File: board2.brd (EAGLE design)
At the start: 100 x 80 mm, 77 parts, among them Q1 7.68MHz, Q2 16MHz

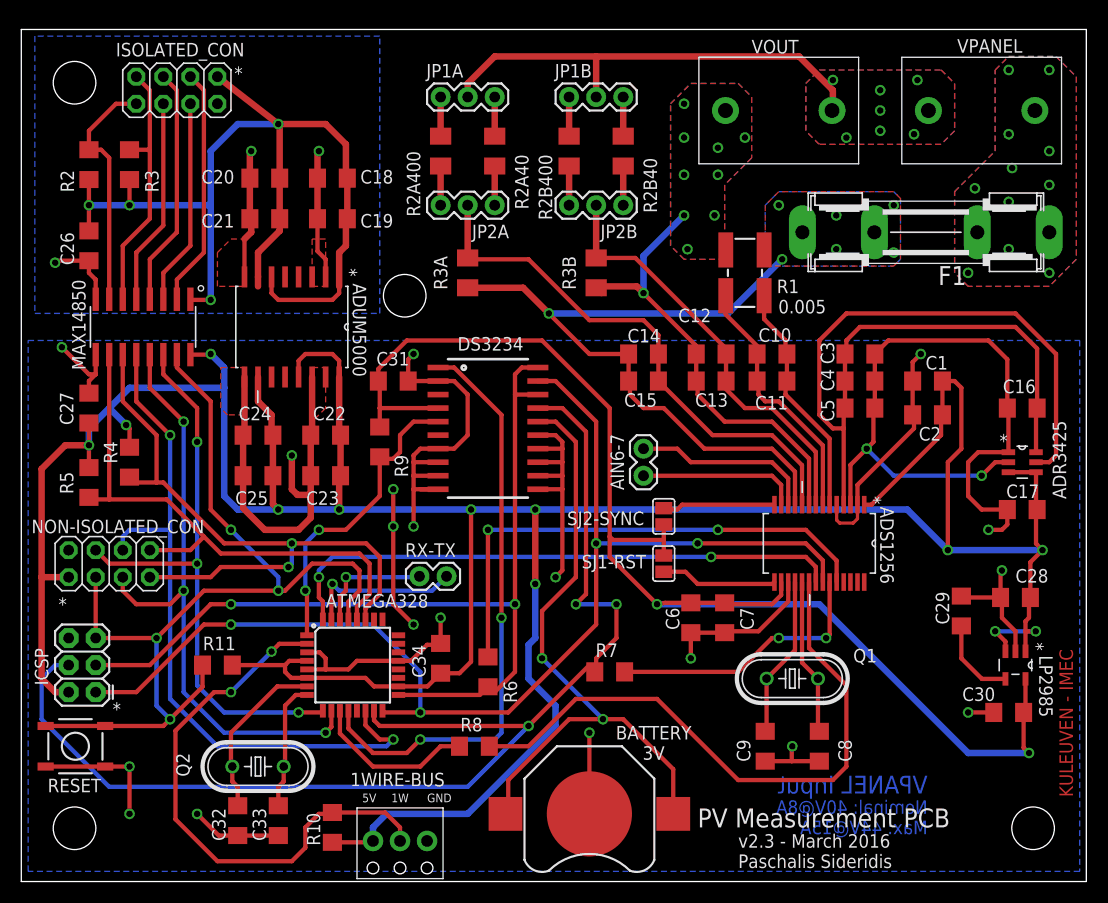
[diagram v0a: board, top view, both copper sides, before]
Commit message: Added RX,TX header, D0-3 pinout. Changed the polygon shape (radius in corners). Created first try in 3D for Inventor.
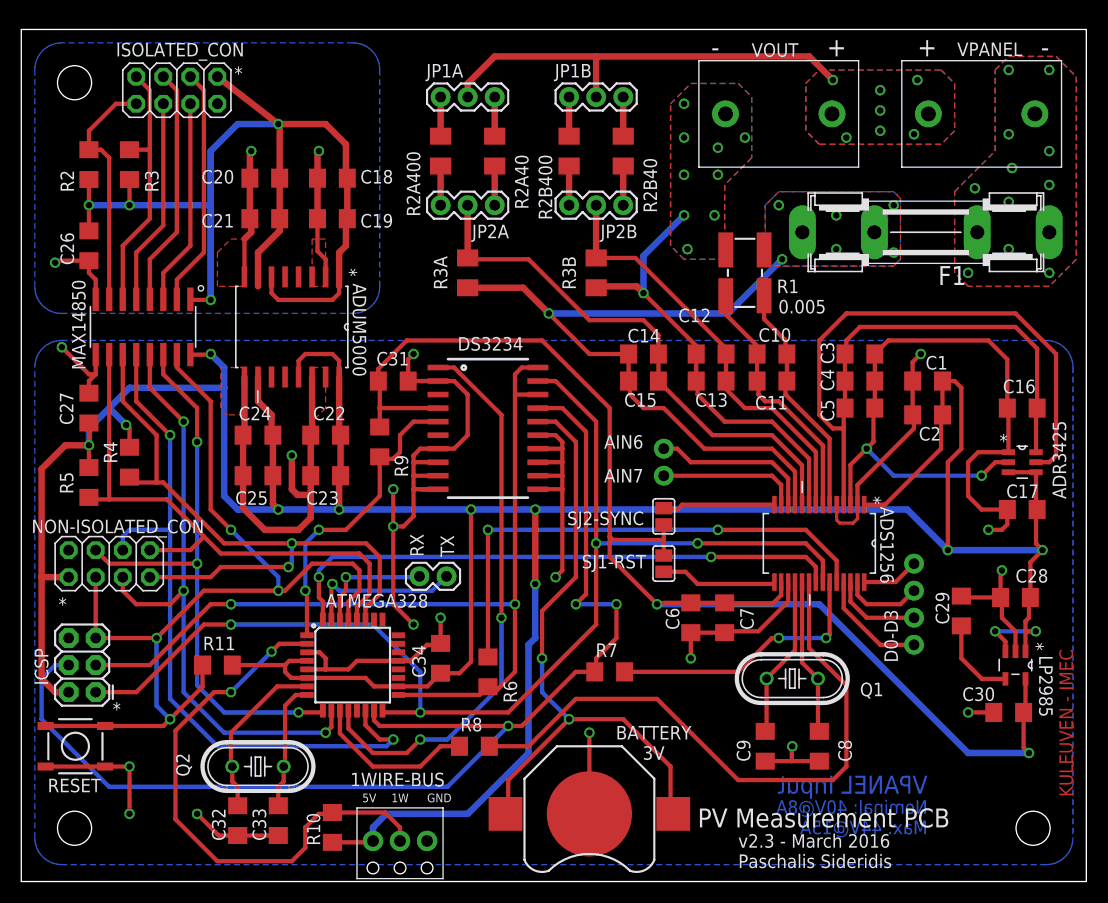
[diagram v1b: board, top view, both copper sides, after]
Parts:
- added D0-D3: (no value), SparkFun-Connectors:1X04_NO_SILK_ALL_ROUND
- AIN6-7: device SparkFun-Connectors:1X02 -> SparkFun-Connectors:1X02_NO_SILK
- moved AIN6-7 3.18 mm to (60.3, 40.6), turned to 270 degrees
- moved VOUT 0.32 mm to (71.1, 72.1)
- moved VPANEL 0.32 mm to (90.2, 72.1)
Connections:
- removed net N$18: ADS1256.12, AIN6-7.2
- removed net N$19: ADS1256.13, AIN6-7.1
- new net AIN6: ADS1256.12, AIN6-7.1
- new net AIN7: ADS1256.13, AIN6-7.2
- new net D0: ADS1256.25, D0-D3.1
- new net D1: ADS1256.26, D0-D3.2
- new net D2: ADS1256.27, D0-D3.3
- new net D3: ADS1256.28, D0-D3.4
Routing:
- net N$18: track 17.2 -> 0.00 mm
- net AIN6: track 0.00 -> 15.3 mm
- net N$19: track 15.1 -> 0.00 mm
- net AIN7: track 0.00 -> 13.2 mm
- net D0: track 0.00 -> 10.5 mm
- net D1: track 0.00 -> 8.43 mm
- net D2: track 0.00 -> 7.41 mm
- net D3: track 0.00 -> 5.39 mm
- net RTC_CS: track 55.4 -> 52.8 mm
- net VBUS1: track 43.7 -> 41.3 mm
- net MOSI: track 115.2 -> 113.5 mm
- net 5V_ISO: track 333.7 -> 332.4 mm
- net GND_ISO: track 275.7 -> 277.1 mm, vias 19 -> 18
- net N$15: track 60.0 -> 58.7 mm
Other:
- board text added: "+"
- board text added: "-"
- board text added: "AIN6"
- board text added: "AIN7"
- board text added: "RX"
- board text added: "TX"

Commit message: Small changes
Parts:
- moved ISOLATED_CON 2.54 mm to (17.1, 74.3)
- moved R3 1.27 mm to (10.2, 66.0)
- moved RESET 0.63 mm to (5.71, 12.7)
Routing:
- net SCL: track 22.8 -> 25.3 mm
- net 5V: track 96.5 -> 95.2 mm
- net OUT1: track 22.5 -> 23.5 mm
- net IN1: track 22.5 -> 23.5 mm
- net SDA: track 24.4 -> 25.5 mm
- net OUT2: track 19.4 -> 20.5 mm
- net IN2: track 19.4 -> 20.5 mm
- net RESET: track 91.2 -> 90.6 mm
- net GND_ISO: track 277.1 -> 277.7 mm

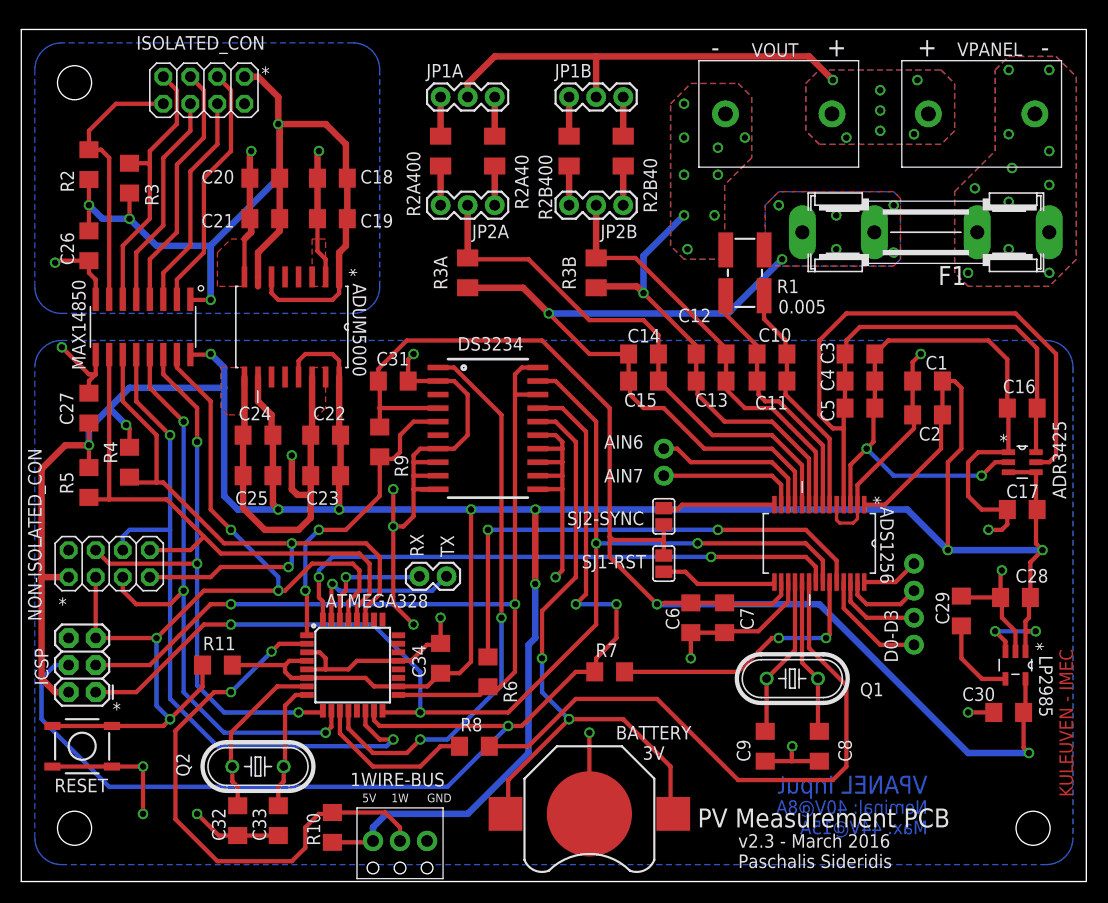
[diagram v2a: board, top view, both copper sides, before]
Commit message: Footprints updated and small changes
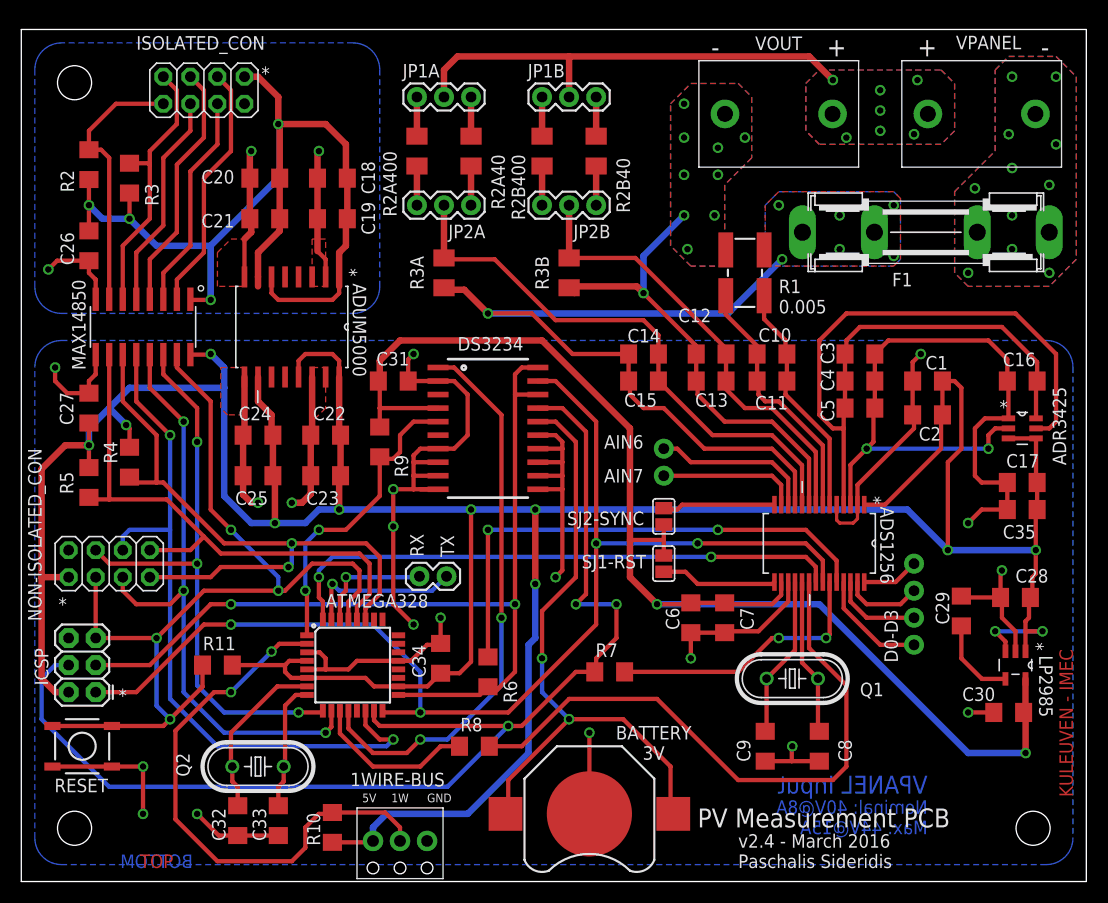
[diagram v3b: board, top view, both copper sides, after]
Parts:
- added C35: 1u, adafruit:C3216
- C34: value 22p -> 0.1u
- VOUT, VPANEL: value 2PIN_TERMINAL_PCBMOUNT -> 2PIN_TERMINAL_PCBMOUNT_10.1MM; device TE CONNECTIVITY:2TERMINALBLOCK_10MMPITCH -> TE CONNECTIVITY:2TERMINALBLOCK_10.1MMPITCH
- moved ADR3425 3.18 mm to (94.0, 42.5)
- moved C17 2.54 mm to (94.0, 37.5)
- moved C16 2.54 mm to (94.0, 47.0)
- moved JP1B 2.54 mm to (48.9, 73.7)
- moved JP2B 2.54 mm to (54.0, 63.5)
- moved R2B40 2.54 mm to (54.0, 68.6)
- moved R2B400 2.54 mm to (48.9, 68.6)
- moved R3B 2.54 mm to (51.4, 57.1)
- moved JP2A 2.22 mm to (42.2, 63.5)
- moved R2A40 2.22 mm to (42.2, 68.6)
- moved JP1A 2.22 mm to (37.1, 73.7)
- moved R2A400 2.22 mm to (37.1, 68.6)
- moved R3A 2.22 mm to (39.7, 57.1)
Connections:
- net 5V_ISO: now also C35.1
- net GND_ISO: now also C35.2
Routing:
- net GND_ISO: track 277.7 -> 262.9 mm, vias 18 -> 19
- net AIN5: track 67.2 -> 75.1 mm
- net VREF_2V5: track 90.9 -> 83.8 mm
- net 5V_ISO: track 332.4 -> 337.4 mm
- net VBUS1: track 41.3 -> 44.3 mm
- net AIN3: track 44.1 -> 46.6 mm
- net AIN2: track 40.4 -> 43.0 mm
- net AIN4: track 50.6 -> 52.9 mm
- net 3V3: track 126.3 -> 124.2 mm
- net GND: track 31.5 -> 32.4 mm
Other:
- board text added: "BOTTOM"
- board text added: "TOP"
- board text added: "v2.4 - March 2016 Paschalis Sideridis"
- board text removed: "v2.3 - March 2016 Paschalis Sideridis"

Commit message: IMPORTANT: Changed the terminals for the PV connectors. They are bigger and with double connections
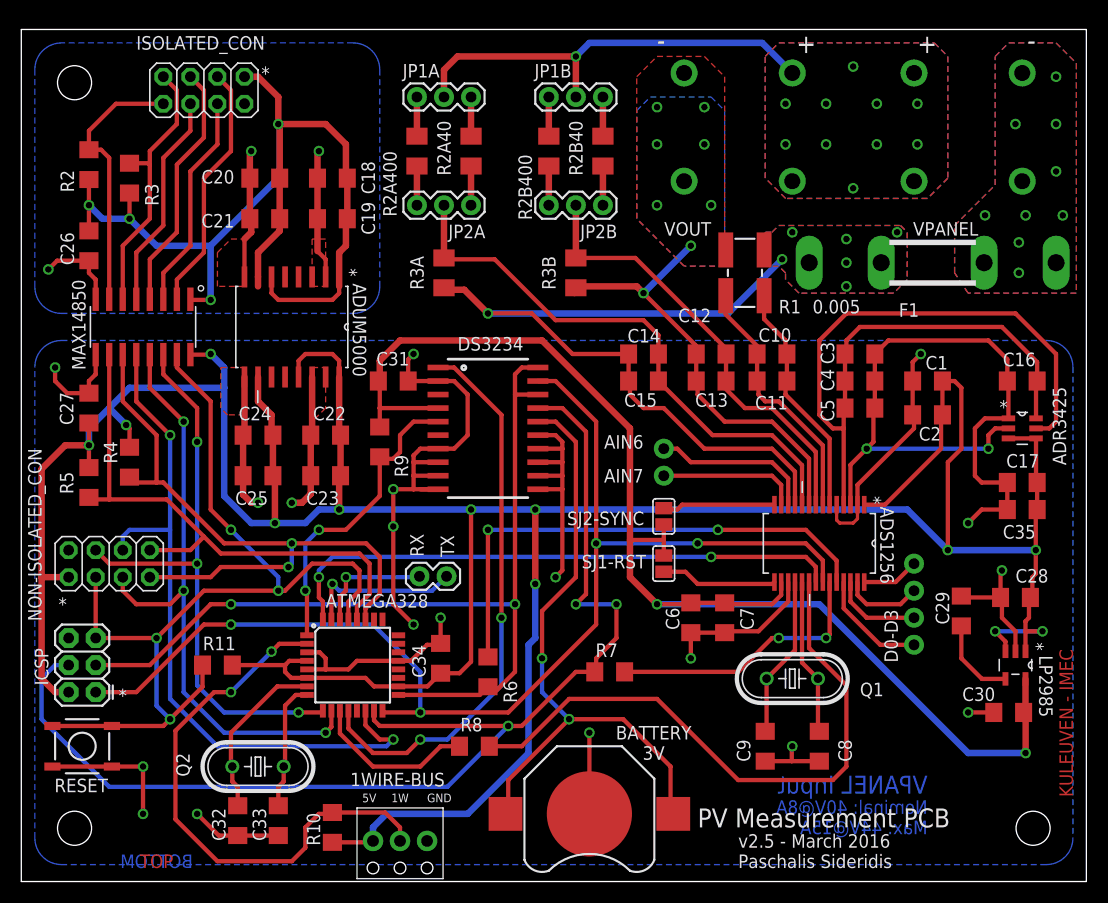
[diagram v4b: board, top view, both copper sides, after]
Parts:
- VOUT, VPANEL: value 2PIN_TERMINAL_PCBMOUNT_10.1MM -> PAS-PHOENIXTERMINAL2PIN-10.16MM; device TE CONNECTIVITY:2TERMINALBLOCK_10.1MMPITCH -> PAS-PHOENIXTERMINAL:PAS-PHOENIXTERMINAL-2PIN-10.16MM
- moved VOUT 3.82 mm to (67.3, 71.8), turned to 180 degrees
- moved F1 2.93 mm to (74.0, 58.1)
- moved VPANEL 1.31 mm to (88.9, 71.8)
- moved JP1B 0.63 mm to (49.5, 73.7)
- moved JP2B 0.63 mm to (54.6, 63.5)
- moved R2B40 0.63 mm to (54.6, 68.6)
- moved R2B400 0.63 mm to (49.5, 68.6)
- moved R3B 0.63 mm to (52.1, 57.1)
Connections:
- net AIN3: now also VOUT.P$3, VOUT.P$4; no longer VOUT.2
- net VBUS1: now also VOUT.P$1, VOUT.P$2, VPANEL.P$3, VPANEL.P$4; no longer VOUT.1, VPANEL.1
- net VBUS2: now also VPANEL.P$1, VPANEL.P$2; no longer VPANEL.2
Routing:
- net AIN3: track 46.6 -> 43.0 mm, vias 10 -> 8
- net VBUS1: track 44.3 -> 41.3 mm, vias 7 -> 11
- net AIN2: track 43.0 -> 42.3 mm
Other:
- board text added: "v2.5 - March 2016 Paschalis Sideridis"
- board text removed: "v2.4 - March 2016 Paschalis Sideridis"

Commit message: Updated connectors and schematic. No big changes
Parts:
- RESET: value TAC_SWITCHSMD -> SWITCH-MOMENTARY-2SMD-4; device SparkFun-Retired:TACTILE-SWITCH-SMD -> SparkFun-Electromechanical:TACTILE_SWITCH_TALL
- moved NON-ISOLATED_CON 2.84 mm to (5.71, 28.6), turned to 90 degrees
- moved ICSP 2.62 mm to (4.45, 17.1), turned to 0 degrees
- moved ISOLATED_CON 1.91 mm to (19.1, 74.3)
- moved RESET 1.71 mm to (6.35, 11.1), turned to 0 degrees
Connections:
- net GND_ISO: now also RESET.A2; no longer RESET.1, RESET.2
- net RESET: now also RESET.B2; no longer RESET.3, RESET.4
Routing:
- net N$25: track 0.00 -> 8.25 mm
- net N$24: track 0.00 -> 7.62 mm
- net MISO: track 112.4 -> 119.5 mm
- net RESET: track 90.6 -> 83.7 mm
- net SDA_ISO: track 62.1 -> 68.0 mm
- net SCLK: track 86.5 -> 91.2 mm
- net OUT2_ISO: track 67.2 -> 71.3 mm
- net MOSI: track 113.5 -> 117.2 mm
- net GND_ISO: track 262.9 -> 259.6 mm
- net IN2_ISO: track 55.3 -> 57.9 mm
- net 5V_ISO: track 337.4 -> 338.5 mm
- net IN1: track 23.5 -> 24.3 mm
- net SDA: track 25.5 -> 26.3 mm
- net OUT2: track 20.5 -> 21.2 mm
- net OUT1: track 23.5 -> 24.3 mm
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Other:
- board text added: "PV Measurements"
- board text added: "RESET"
- board text added: "v2.6 - April 2016 Paschalis Sideridis"
- board text removed: "PV Measurement PCB"
- board text removed: "v2.5 - March 2016 Paschalis Sideridis"

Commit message: Small changes
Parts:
- added LED1: (no value), adafruit:CHIPLED_0805
- added R12: 1k, adafruit:R3216
- moved C34 1.42 mm to (40.6, 20.3)
- moved JP2A 1.27 mm to (43.5, 63.5)
- moved R2A40 1.27 mm to (43.5, 68.6)
- moved R3A 1.27 mm to (41.0, 57.1)
- moved RX-TX 1.27 mm to (38.7, 28.7)
- moved JP1A 1.27 mm to (38.4, 73.7)
- moved R2A400 1.27 mm to (38.4, 68.6)
- moved C8 0.95 mm to (74.9, 13.7)
- moved C9 0.95 mm to (69.8, 13.7)
- moved R6 0.90 mm to (44.5, 19.1)
- moved R11 0.64 mm to (18.4, 19.7)
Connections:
- new net N$18: ATMEGA328.24, R12.1
- new net N$19: LED1.A, R12.2
- net GND_ISO: now also LED1.C
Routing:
- net N$18: track 0.00 -> 15.5 mm
- net AIN5: track 75.1 -> 68.7 mm
- net SCLK: track 91.2 -> 94.3 mm
- net N$19: track 0.00 -> 2.25 mm
- net GND_ISO: track 259.6 -> 260.8 mm
- net AIN4: track 52.9 -> 51.6 mm
- net VBUS1: track 41.6 -> 40.3 mm
- net TX: track 14.9 -> 16.2 mm
- net N$16: track 57.8 -> 56.6 mm
- net RX: track 11.1 -> 12.4 mm
- net RTC_CS: track 52.8 -> 53.9 mm
- net N$12: track 15.2 -> 14.2 mm
- net N$11: track 14.7 -> 13.7 mm
- net 5V_ISO: track 338.5 -> 339.3 mm
- net RESET: track 83.7 -> 83.1 mm
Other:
- board text added: "v2.7 - April 2016 Paschalis Sideridis"
- board text removed: "v2.6 - April 2016 Paschalis Sideridis"

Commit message: FINAL BOARD AS ORDERED - v2.7
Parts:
- moved JP2A 0.64 mm to (42.9, 63.5)
- moved R2A40 0.64 mm to (42.9, 68.6)
- moved R3A 0.64 mm to (40.3, 57.1)
- moved C30 0.63 mm to (92.7, 15.2)
- moved JP1A 0.63 mm to (37.8, 73.7)
- moved JP1B 0.63 mm to (48.9, 73.7)
- moved JP2B 0.63 mm to (54.0, 63.5)
- moved R2A400 0.63 mm to (37.8, 68.6)
- moved R2B40 0.63 mm to (54.0, 68.6)
- moved R2B400 0.63 mm to (48.9, 68.6)
- moved R3B 0.63 mm to (51.4, 57.1)
- renumbered SJ1-RST to RST, SJ2-SYNC to SYNC
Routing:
- net RESET: track 83.1 -> 92.2 mm, vias 4 -> 5
- net GND_ISO: track 260.8 -> 257.0 mm
- net 5V_ISO: track 339.3 -> 342.6 mm, vias 12 -> 13
- net 3V3: track 124.2 -> 126.7 mm, vias 2 -> 3
- net AIN5: track 68.7 -> 70.6 mm
- net 1WIRE_BUS: track 51.6 -> 49.8 mm
- net AIN3: track 43.0 -> 44.1 mm
- net 5V: track 95.0 -> 94.1 mm
- net AIN4: track 51.6 -> 52.2 mm
- net VBUS1: track 40.3 -> 41.0 mm
- net AIN2: track 42.3 -> 43.0 mm
- net SCLK: track 94.3 -> 94.9 mm
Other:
- board text added: "3V3"
- board text added: "BATTERY RTC 3V"
- board text added: "RST"
- board text added: "SHUNT"
- board text removed: "BATTERY 3V"
